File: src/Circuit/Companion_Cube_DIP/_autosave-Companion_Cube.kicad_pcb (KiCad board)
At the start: 2 copper layers, 43.2 x 43.2 mm, 21 parts, among them CON1 AVR-ISP-6, IC1 ATTINY85-S, P1 LED_4, P2 LED_3, P3 LED_2, P4 LED_1, P5 CONN_1, P6 CONN_1, P7 CONN_1, U1 MINI-B_USB

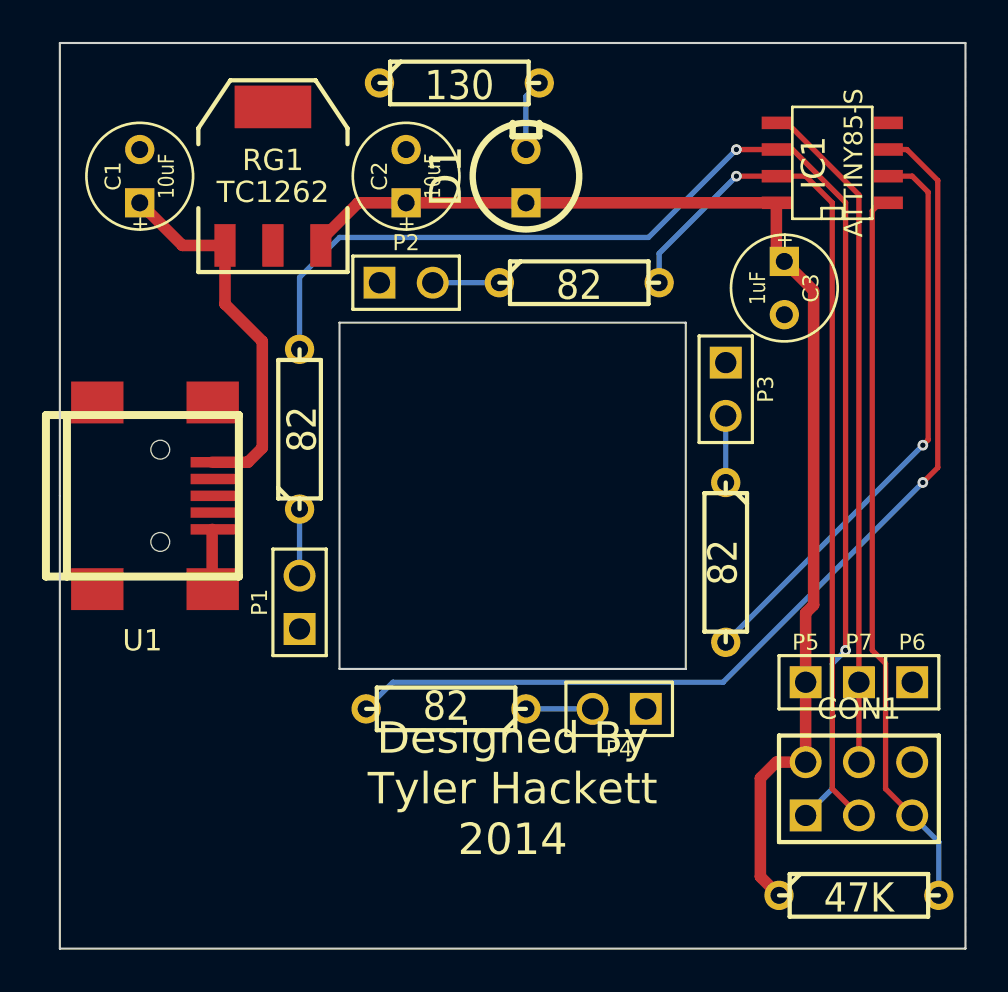
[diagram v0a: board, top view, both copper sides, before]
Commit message: Added attiny85 DIP version
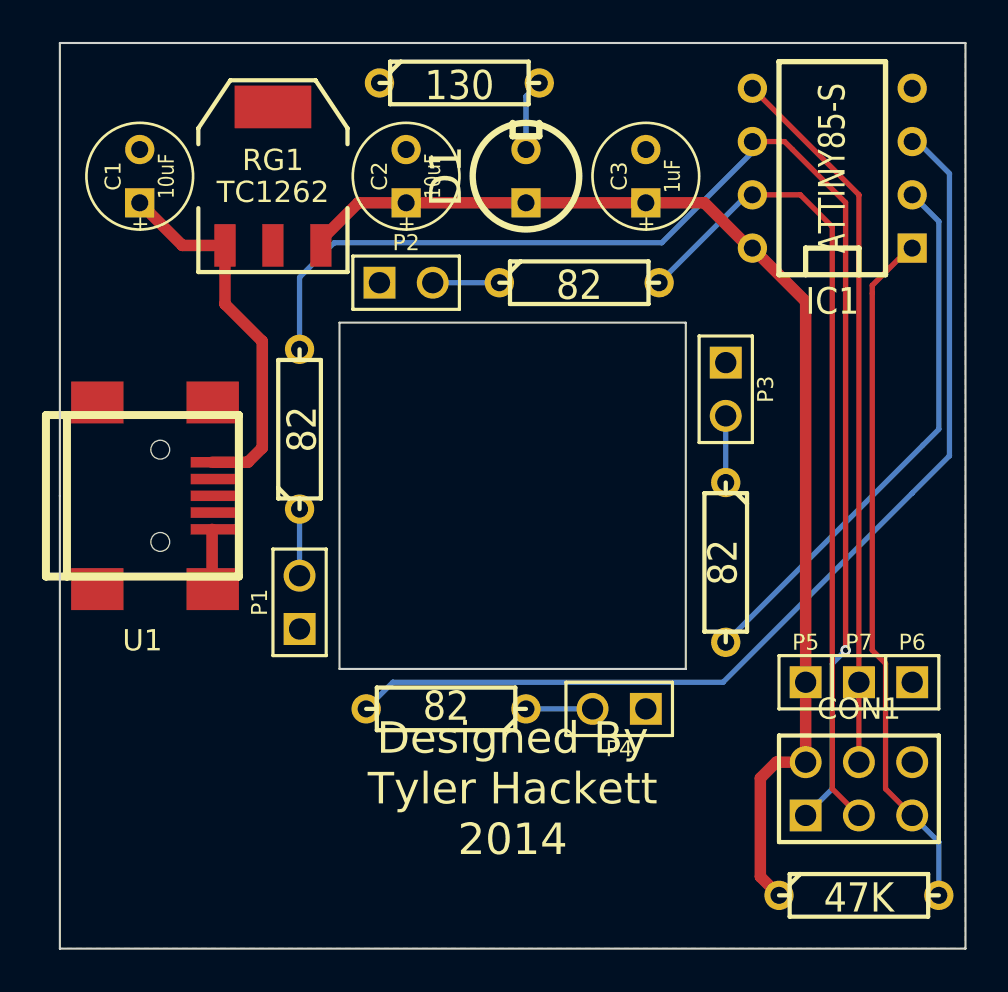
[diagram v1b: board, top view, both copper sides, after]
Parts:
- IC1: footprint SO8E -> DIP-8__300
- moved C3 8.49 mm to (205.7, 115.6), turned to 90 degrees
- moved IC1 0.25 mm to (214.6, 115.2)
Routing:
- net VCC: track 58.7 -> 56.5 mm
- net N-000006: track 41.4 -> 39.3 mm, vias 1 -> 0
- net N-000002: track 34.9 -> 33.0 mm
- net N-000003: track 32.4 -> 34.2 mm
- net N-000005: track 27.7 -> 26.1 mm, vias 1 -> 0
- net N-000007: track 63.0 -> 63.9 mm, vias 2 -> 1
- net N-000004: vias 1 -> 0
